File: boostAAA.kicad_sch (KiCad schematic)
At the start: 10 parts, among them SW1 EN, U1 MCP1642B-50I/MS

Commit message: Various final tweaks
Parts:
- BT1: Farnell (none) -> 3126578
- C1, C2: Farnell (none) -> 3013456
- H1, H2, SW1, TP1, TP2: Farnell (none) -> -
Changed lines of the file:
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@@
+      (effects (font (size 1.27 1.27)) hide)
+    )
+    (property "Farnell" "-" (id 4) (at 123.19 58.42 0)
       (effects (font (size 1.27 1.27)) hide)
     )
@@
       (effects (font (size 1.27 1.27)) hide)
     )
+    (property "Farnell" "-" (id 4) (at 81.28 68.58 0)
+      (effects (font (size 1.27 1.27)) hide)
+    )
     (pin "1")
     (pin "2")
@@
       (effects (font (size 1.27 1.27)) hide)
     )
+    (property "Farnell" "3013456" (id 4) (at 77.47 55.88 0)
+      (effects (font (size 1.27 1.27)) hide)
+    )
     (pin "1")
     (pin "2")
@@
       (effects (font (size 1.27 1.27)) hide)
     )
+    (property "Farnell" "-" (id 4) (at 123.19 53.34 0)
+      (effects (font (size 1.27 1.27)) hide)
+    )
     (pin "1")
   )
@@
       (effects (font (size 1.27 1.27)) hide)
     )
+    (property "Farnell" "-" (id 4) (at 114.3 73.66 0)
+      (effects (font (size 1.27 1.27)) hide)
+    )
   )
   (symbol (lib_id "Mechanical:MountingHole") (at 114.3 78.74 0) (unit 1)
@@
     )
     (property "Datasheet" "~" (id 3) (at 114.3 78.74 0)
+      (effects (font (size 1.27 1.27)) hide)
+    )
+    (property "Farnell" "-" (id 4) (at 114.3 78.74 0)
       (effects (font (size 1.27 1.27)) hide)
     )
@@
       (effects (font (size 1.27 1.27)) hide)
     )
+    (property "Farnell" "3126578" (id 4) (at 68.58 58.42 0)
+      (effects (font (size 1.27 1.27)) hide)
+    )
     (pin "1")
     (pin "2")
@@
       (effects (font (size 1.27 1.27)) hide)
     )
+    (property "Farnell" "3013456" (id 4) (at 118.11 55.88 0)
+      (effects (font (size 1.27 1.27)) hide)
+    )

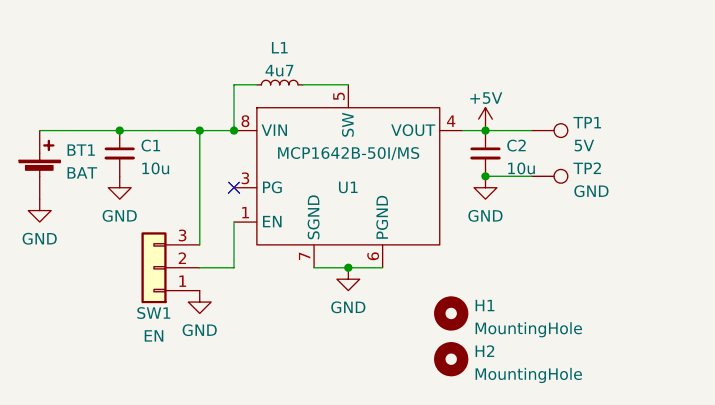
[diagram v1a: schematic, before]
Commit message: Updated version to use autogen for library symbols and to allow for the use of adjustable as well as fixed versions of the regulator chip.
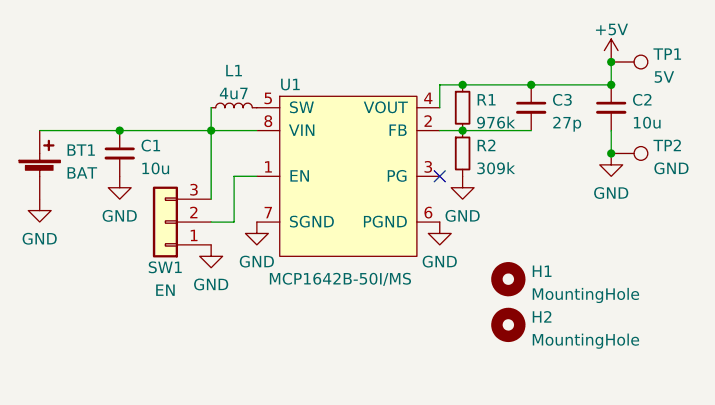
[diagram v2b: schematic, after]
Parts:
- added C3: 27p, Capacitor_SMD:C_0603_1608Metric, symbol Device:C_Small
- added R1: 976k, Resistor_SMD:R_0603_1608Metric, symbol Device:R_Small
- added R2: 309k, Resistor_SMD:R_0603_1608Metric, symbol Device:R_Small
- SW1: footprint battery-booster:EN_SW -> boostAAA:EN_SW
- U1: symbol battery-booster:MCP1642B-50I/MS -> boostAAA:MCP1642B-50I/MS
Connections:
- net +5V: now also C3.1, R1.1
- net GND: now also R2.2
- net at U1.2 (FB): now also C3.2, R1.2, R2.1
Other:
- moved on the sheet: C2, H1, H2, L1, SW1, TP1, TP2

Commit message: LCSC Part Numbers and BOM
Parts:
- C1, C2: LCSC (none) -> C1713
- L1: LCSC (none) -> C340369
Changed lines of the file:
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@@
+      (effects (font (size 1.27 1.27)) hide)
+    )
+    (property "LCSC" "C1713" (id 5) (at 77.47 55.88 0)
       (effects (font (size 1.27 1.27)) hide)
     )
@@
     )
     (property "Farnell" "2771305" (id 4) (at 90.17 50.8 90)
+      (effects (font (size 1.27 1.27)) hide)
+    )
+    (property "LCSC" "C340369" (id 5) (at 90.17 50.8 0)
       (effects (font (size 1.27 1.27)) hide)
     )
@@
       (effects (font (size 1.27 1.27)) hide)
     )
+    (property "LCSC" "C1713" (id 5) (at 132.08 50.8 0)
+      (effects (font (size 1.27 1.27)) hide)
+    )
